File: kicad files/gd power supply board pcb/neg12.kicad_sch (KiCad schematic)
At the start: 21 parts, among them U1 MAX17580

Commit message: pre-routing try 1
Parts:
- removed R4: 0, Resistor_SMD:R_0805_2012Metric, symbol My Library:R_0805
- removed R6: 1k, Resistor_SMD:R_0805_2012Metric, symbol My Library:R_0805
- removed TP1, TP2, TP4: TestPoint_Harwin, My Libraries:Harwin-S1751-46-Test-Point, symbol My Library:TestPoint_Harwin
- added C9: 1u, Capacitor_SMD:C_0805_2012Metric, symbol My Library:C_0805
- added JP3: neg_12_jmp, Jumper:SolderJumper-2_P1.3mm_Open_TrianglePad1.0x1.5mm, symbol Jumper:Jumper_2_Open
- C4: footprint Capacitor_SMD:C_0805_2012Metric -> Capacitor_SMD:C_0603_1608Metric
- R1: footprint Resistor_SMD:R_0805_2012Metric -> Resistor_SMD:R_0402_1005Metric
- TP5, TP6, TP8: footprint My Libraries:Harwin-S1751-46-Test-Point -> TestPoint:TestPoint_Pad_1.0x1.0mm
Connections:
- net FB: now also R3.2
- net GND: now also C9.2
- net Neg12_Out: now also R5.2, C9.1
- net Vin: now also JP3.1 (A); no longer C2.1, U1.1 (In)
- new net neg12_Vin: C2.1, JP3.2 (B), U1.1 (In)
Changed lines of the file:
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@@
   (junction (at 146.05 74.93) (diameter 0) (color 0 0 0 0)
   )
-  (junction (at 105.41 99.06) (diameter 0) (color 0 0 0 0)
-  )
   (junction (at 92.71 74.93) (diameter 0) (color 0 0 0 0)
   )
@@
   (junction (at 128.27 115.57) (diameter 0) (color 0 0 0 0)
   )
-  (junction (at 86.36 87.63) (diameter 0) (color 0 0 0 0)
-  )
-  (junction (at 95.25 92.71) (diameter 0) (color 0 0 0 0)
-  )
   (junction (at 179.07 115.57) (diameter 0) (color 0 0 0 0)
   )
@@
     (stroke (width 0) (type default) (color 0 0 0 0))
   )
+  (wire (pts (xy 179.07 109.22) (xy 184.15 109.22))
+    (stroke (width 0) (type default) (color 0 0 0 0))
+  )
   (wire (pts (xy 179.07 88.9) (xy 179.07 92.71))
     (stroke (width 0) (type default) (color 0 0 0 0))
@@
     (stroke (width 0) (type default) (color 0 0 0 0))
   )
+  (wire (pts (xy 179.07 95.25) (xy 184.15 95.25))
+    (stroke (width 0) (type default) (color 0 0 0 0))
+  )
   (wire (pts (xy 163.83 88.9) (xy 167.64 88.9))
     (stroke (width 0) (type default) (color 0 0 0 0))
@@
     (stroke (width 0) (type default) (color 0 0 0 0))
   )
-  (wire (pts (xy 92.71 74.93) (xy 86.36 74.93))
+  (wire (pts (xy 80.01 74.93) (xy 92.71 74.93))
     (stroke (width 0) (type default) (color 0 0 0 0))
   )
@@
   )
   (wire (pts (xy 92.71 81.28) (xy 92.71 82.55))
+    (stroke (width 0) (type default) (color 0 0 0 0))
+  )
+  (wire (pts (xy 67.31 74.93) (xy 69.85 74.93))
     (stroke (width 0) (type default) (color 0 0 0 0))
   )
@@
     (effects (font (size 1.27 1.27)) (justify right bottom))
   )
+  (label "neg12_Vin" (at 92.71 74.93 0)
+    (effects (font (size 1.27 1.27)) (justify left bottom))
+  )
   (label "~{RESET}" (at 149.86 96.52 180)
     (effects (font (size 1.27 1.27)) (justify right bottom))
@@
     (effects (font (size 1.27 1.27)) (justify left))
   )
+  (hierarchical_label "Vin" (shape input) (at 67.31 74.93 180)
+    (effects (font (size 1.27 1.27)) (justify right))
+  )
   (hierarchical_label "Neg12_Out" (shape input) (at 199.39 115.57 0)
     (effects (font (size 1.27 1.27)) (justify left))
   )
-  (hierarchical_label "Vin" (shape input) (at 86.36 74.93 180)
-    (effects (font (size 1.27 1.27)) (justify right))
-  )
   (symbol (lib_id "My Library:TestPoint_Harwin") (at 146.05 74.93 0) (unit 1)
     (in_bom yes) (on_board yes)
@@
       (effects (font (size 1.27 1.27)) hide)
     )
-    (property "Footprint" "My Libraries:Harwin-S1751-46-Test-Point" (id 2) (at 151.13 74.93 0)
+    (property "Footprint" "TestPoint:TestPoint_Pad_1.0x1.0mm" (id 2) (at 151.13 74.93 0)
       (effects (font (size 1.27 1.27)) hide)
     )
@@
     )
     (pin "1")
-  )
-  (symbol (lib_id "My Library:R_0805") (at 181.61 109.22 90) (unit 1)
-    (in_bom yes) (on_board yes)
-    (property "Reference" "R6" (id 0) (at 181.61 109.22 90))
-    (property "Value" "1k" (id 1) (at 186.69 109.22 90))
-    (property "Footprint" "Resistor_SMD:R_0805_2012Metric" (id 2) (at 181.61 109.22 0)
-      (effects (font (size 1.27 1.27)) hide)
-    )
-    (property "Datasheet" "~" (id 3) (at 181.61 109.22 0)
-      (effects (font (size 1.27 1.27)) hide)
-    )
-    (pin "1")
-    (pin "2")
   )
   (symbol (lib_id "My Library:TestPoint_Harwin") (at 184.15 101.6 270) (unit 1)
@@
       (effects (font (size 1.27 1.27)) hide)
     )
-    (property "Footprint" "My Libraries:Harwin-S1751-46-Test-Point" (id 2) (at 184.15 106.68 0)
+    (property "Footprint" "TestPoint:TestPoint_Pad_1.0x1.0mm" (id 2) (at 184.15 106.68 0)
       (effects (font (size 1.27 1.27)) hide)
     )
@@
     (pin "1")
   )
+  (symbol (lib_id "My Library:C_0805") (at 123.19 118.11 0) (unit 1)
+    (in_bom yes) (on_board yes) (fields_autoplaced)
+    (property "Reference" "C9" (id 0) (at 125.73 116.8462 0)
+      (effects (font (size 1.27 1.27)) (justify left))
+    )
+    (property "Value" "1u" (id 1) (at 125.73 119.3862 0)
+      (effects (font (size 1.27 1.27)) (justify left))
+    )
+    (property "Footprint" "Capacitor_SMD:C_0805_2012Metric" (id 2) (at 123.19 118.11 0)
+      (effects (font (size 1.27 1.27)) hide)
+    )
+    (property "Datasheet" "~" (id 3) (at 123.19 118.11 0)
+      (effects (font (size 1.27 1.27)) hide)
+    )
+    (pin "1")
+    (pin "2")
+  )
   (symbol (lib_id "My Library:C_0805") (at 167.64 101.6 0) (unit 1)
     (in_bom yes) (on_board yes) (fields_autoplaced)
@@
     (pin "1")
   )
-  (symbol (lib_id "My Library:TestPoint_Harwin") (at 105.41 99.06 90) (unit 1)
-    (in_bom yes) (on_board yes)
-    (property "Reference" "TP4" (id 0) (at 102.87 97.79 90))
-    (property "Value" "TestPoint_Harwin" (id 1) (at 100.33 99.06 0)
-      (effects (font (size 1.27 1.27)) hide)
-    )
-    (property "Footprint" "My Libraries:Harwin-S1751-46-Test-Point" (id 2) (at 105.41 93.98 0)
-      (effects (font (size 1.27 1.27)) hide)
-    )
-    (property "Datasheet" "~" (id 3) (at 105.41 93.98 0)
-      (effects (font (size 1.27 1.27)) hide)
-    )
-    (pin "1")
-  )
   (symbol (lib_id "My Library:C_0805") (at 143.51 85.09 0) (unit 1)
     (in_bom yes) (on_board yes) (fields_autoplaced)
@@
       (effects (font (size 1.27 1.27)) (justify left))
     )
-    (property "Footprint" "Capacitor_SMD:C_0805_2012Metric" (id 2) (at 143.51 85.09 0)
+    (property "Footprint" "Capacitor_SMD:C_0603_1608Metric" (id 2) (at 143.51 85.09 0)
       (effects (font (size 1.27 1.27)) hide)
     )
@@
       (effects (font (size 1.27 1.27)) (justify left))
     )
-    (property "Footprint" "Resistor_SMD:R_0805_2012Metric" (id 2) (at 105.41 106.68 0)
+    (property "Footprint" "Resistor_SMD:R_0402_1005Metric" (id 2) (at 105.41 106.68 0)
       (effects (font (size 1.27 1.27)) hide)
     )
@@
     (pin "2")
   )
-  (symbol (lib_id "My Library:TestPoint_Harwin") (at 86.36 87.63 90) (unit 1)
-    (in_bom yes) (on_board yes)
-    (property "Reference" "TP1" (id 0) (at 81.28 87.63 0))
-    (property "Value" "TestPoint_Harwin" (id 1) (at 81.28 87.63 0)
-      (effects (font (size 1.27 1.27)) hide)
-    )
-    (property "Footprint" "My Libraries:Harwin-S1751-46-Test-Point" (id 2) (at 86.36 82.55 0)
-      (effects (font (size 1.27 1.27)) hide)
-    )
-    (property "Datasheet" "~" (id 3) (at 86.36 82.55 0)
-      (effects (font (size 1.27 1.27)) hide)
-    )
-    (pin "1")
+  (symbol (lib_id "Jumper:Jumper_2_Open") (at 74.93 74.93 0) (unit 1)
+    (in_bom yes) (on_board yes) (fields_autoplaced)
+    (property "Reference" "JP3" (id 0) (at 74.93 68.58 0))
+    (property "Value" "neg_12_jmp" (id 1) (at 74.93 71.12 0))
+    (property "Footprint" "Jumper:SolderJumper-2_P1.3mm_Open_TrianglePad1.0x1.5mm" (id 2) (at 74.93 74.93 0)
+      (effects (font (size 1.27 1.27)) hide)
+    )
+    (property "Datasheet" "~" (id 3) (at 74.93 74.93 0)
+      (effects (font (size 1.27 1.27)) hide)
+    )
+    (pin "1")
+    (pin "2")
   )
   (symbol (lib_id "My Library:TestPoint_Harwin") (at 143.51 96.52 180) (unit 1)
@@
       (effects (font (size 1.27 1.27)) hide)
     )
-    (property "Footprint" "My Libraries:Harwin-S1751-46-Test-Point" (id 2) (at 138.43 96.52 0)
+    (property "Footprint" "TestPoint:TestPoint_Pad_1.0x1.0mm" (id 2) (at 138.43 96.52 0)
       (effects (font (size 1.27 1.27)) hide)
     )
@@
     (pin "2")
   )
-  (symbol (lib_id "My Library:R_0805") (at 181.61 95.25 90) (unit 1)
-    (in_bom yes) (on_board yes)
-    (property "Reference" "R4" (id 0) (at 181.61 95.25 90))
-    (property "Value" "0" (id 1) (at 186.69 95.25 90))
-    (property "Footprint" "Resistor_SMD:R_0805_2012Metric" (id 2) (at 181.61 95.25 0)
-      (effects (font (size 1.27 1.27)) hide)
-    )
-    (property "Datasheet" "~" (id 3) (at 181.61 95.25 0)
-      (effects (font (size 1.27 1.27)) hide)
-    )
-    (pin "1")
-    (pin "2")
-  )
-  (symbol (lib_id "My Library:TestPoint_Harwin") (at 95.25 92.71 90) (unit 1)
-    (in_bom yes) (on_board yes)
-    (property "Reference" "TP2" (id 0) (at 90.17 92.71 0))
-    (property "Value" "TestPoint_Harwin" (id 1) (at 90.17 92.71 0)
-      (effects (font (size 1.27 1.27)) hide)
-    )
-    (property "Footprint" "My Libraries:Harwin-S1751-46-Test-Point" (id 2) (at 95.25 87.63 0)
-      (effects (font (size 1.27 1.27)) hide)
-    )
-    (property "Datasheet" "~" (id 3) (at 95.25 87.63 0)
-      (effects (font (size 1.27 1.27)) hide)
-    )
+  (symbol (lib_id "power:GND") (at 123.19 120.65 0) (unit 1)
+    (in_bom yes) (on_board yes) (fields_autoplaced)
+    (property "Reference" "#PWR0119" (id 0) (at 123.19 127 0)
+      (effects (font (size 1.27 1.27)) hide)
+    )
+    (property "Value" "GND" (id 1) (at 123.19 125.73 0)
+      (effects (font (size 1.27 1.27)) hide)
+    )
+    (property "Footprint" "" (id 2) (at 123.19 120.65 0)
+      (effects (font (size 1.27 1.27)) hide)
+    )
+    (property "Datasheet" "" (id 3) (at 123.19 120.65 0)
+      (effects (font (size 1.27 1.27)) hide)
+    )

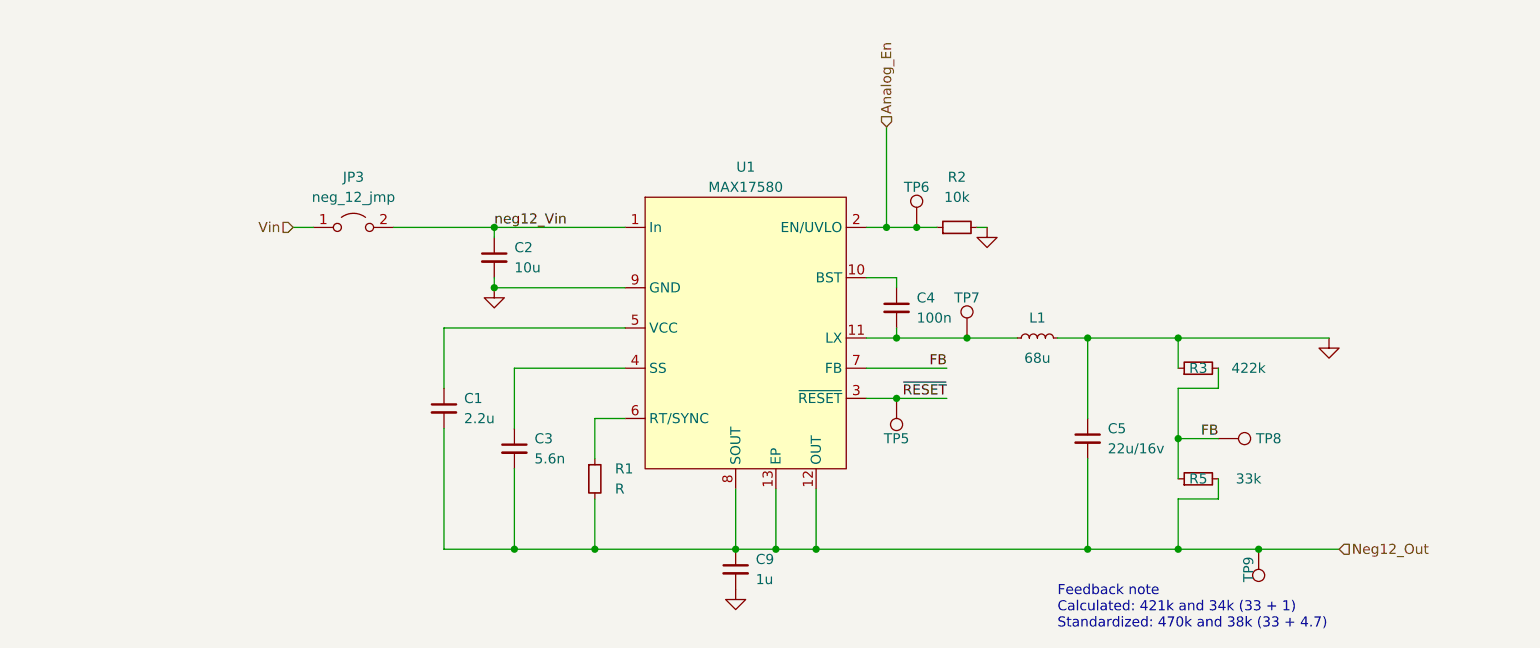
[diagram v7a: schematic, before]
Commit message: added filters and ripped up the board
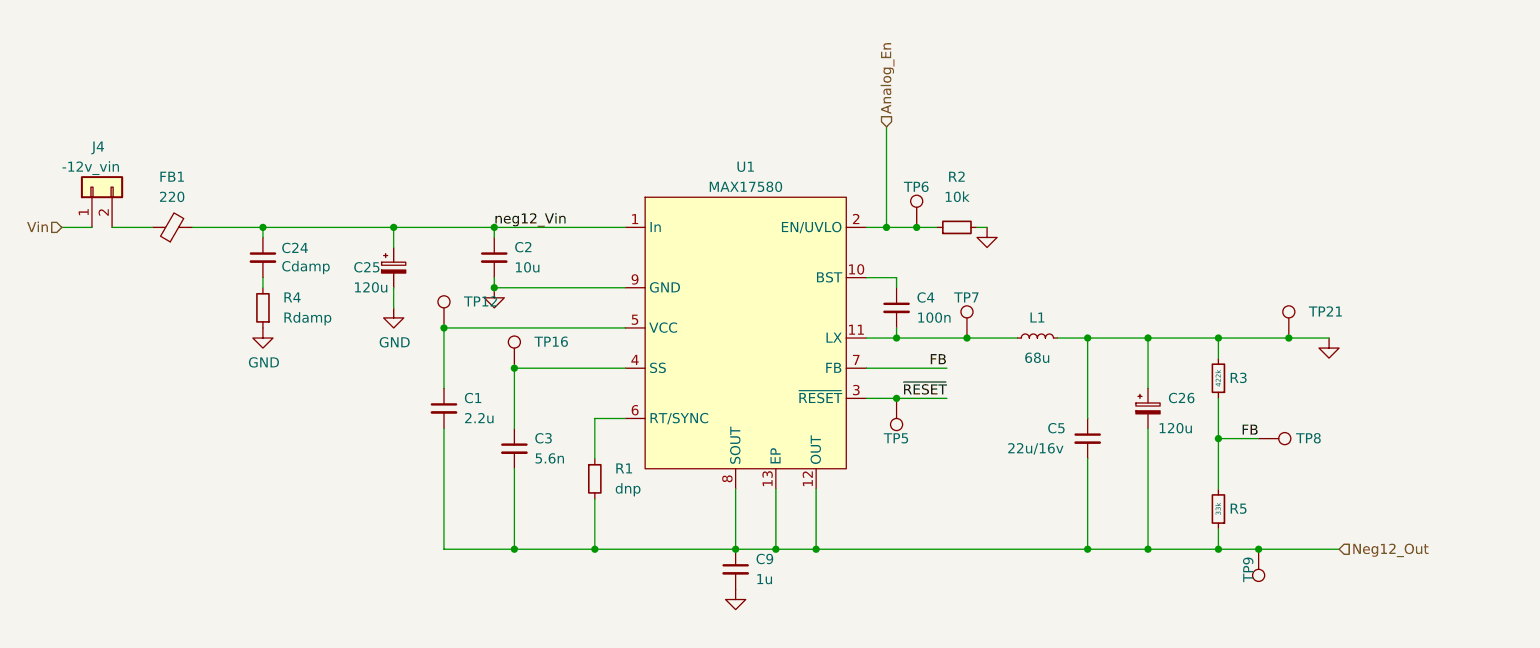
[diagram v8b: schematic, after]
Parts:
- removed JP3: neg_12_jmp, Jumper:SolderJumper-2_P1.3mm_Open_TrianglePad1.0x1.5mm, symbol Jumper:Jumper_2_Open
- added C24: Cdamp, Capacitor_SMD:C_0805_2012Metric_Pad1.18x1.45mm_HandSolder, symbol Device:C_Small
- added C25, C26: 120u, Capacitor_THT:CP_Radial_D8.0mm_P3.80mm, symbol Device:C_Polarized_Small
- added FB1: 220, Inductor_SMD:L_0603_1608Metric_Pad1.05x0.95mm_HandSolder, symbol Device:FerriteBead_Small
- added J4: -12v_vin, Connector_PinHeader_2.54mm:PinHeader_1x02_P2.54mm_Vertical, symbol Connector_Generic:Conn_01x02
- added R4: Rdamp, Resistor_SMD:R_0805_2012Metric_Pad1.20x1.40mm_HandSolder, symbol My Library:R_0805
- added TP12, TP16, TP21: TestPoint_Harwin, TestPoint:TestPoint_Pad_1.0x1.0mm, symbol My Library:TestPoint_Harwin
- R1: value R -> dnp
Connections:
- net FB: now also R3.1, R5.2; no longer R3.2, R5.1
- net GND: now also R3.2, C25.2, C26.1, R4.1, TP21.1; no longer R3.1
- net Neg12_Out: now also R5.1, C26.2; no longer R5.2
- net Vin: now also J4.1 (Pin_1)
- net neg12_Vin: now also C24.1, C25.1, FB1.2
- net at C1.1, U1.5 (VCC): now also TP12.1
- net at C3.1, U1.4 (SS): now also TP16.1
- new net: FB1.1, J4.2 (Pin_2)
- new net: C24.2, R4.2
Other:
- note removed: "Feedback note Calculated: 421k and 34k (33 + 1) Standardized: 470k and 38k (33 + 4.7)"
- moved on the sheet: R3, R5, TP8
